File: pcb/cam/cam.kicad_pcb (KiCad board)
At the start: 4 copper layers, 75 x 65 mm, 116 parts, among them J1 Conn_Coaxial, J2 Power In, J3 PRGR, J4 Conn_01x24_Male, J5 SIM_Card, J6 Conn_Coaxial, J7 JTAG, Q1 IRLML6402, U1 TPS22810, U10 W25Q128JVS, U11 LY68L6400, U12 SRV05-4, U13 SIM800C, U2 FDC610, U3 XC6206-12, U4 XC6206-28, U5 LTC3103, U6 INA226, U7 ESP32-S2, U8 MP2307, Y1 32.768kHz, Y2 40Mhz

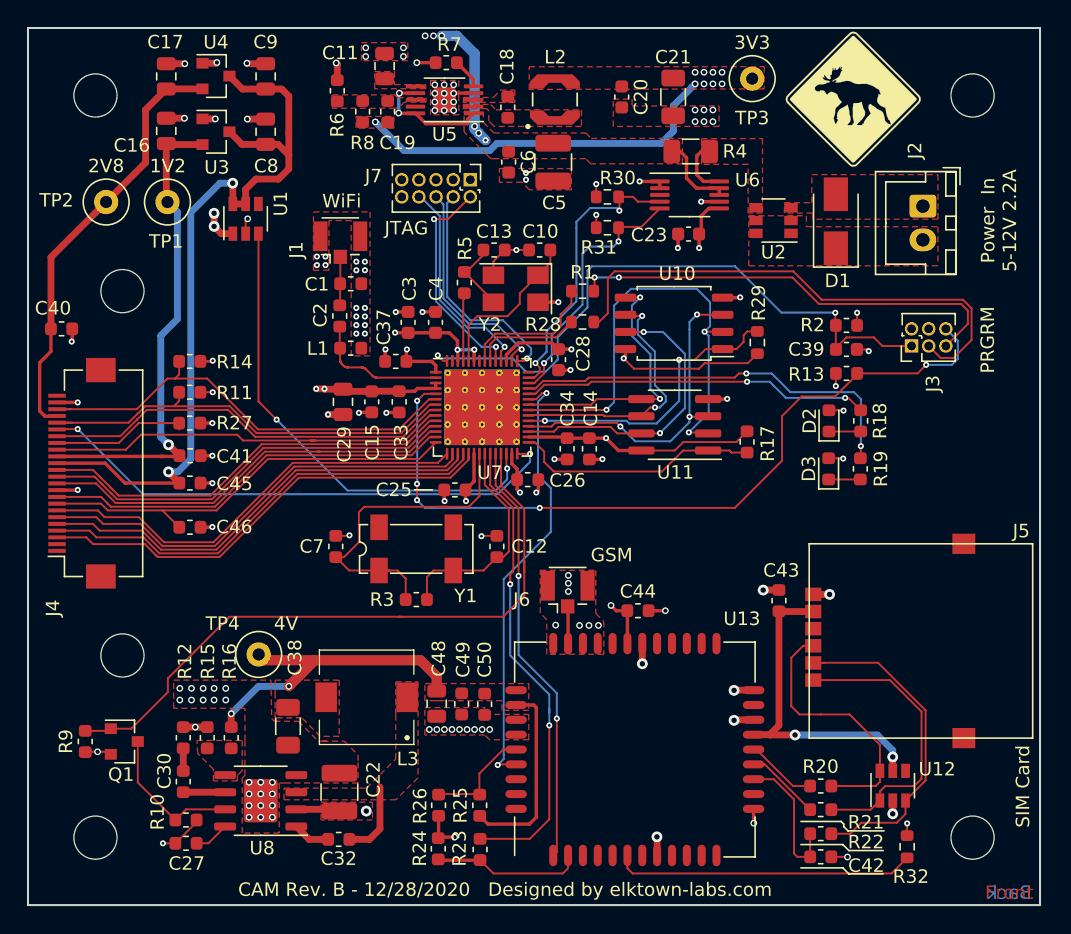
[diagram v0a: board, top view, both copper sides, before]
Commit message: Migrated to KiCad7
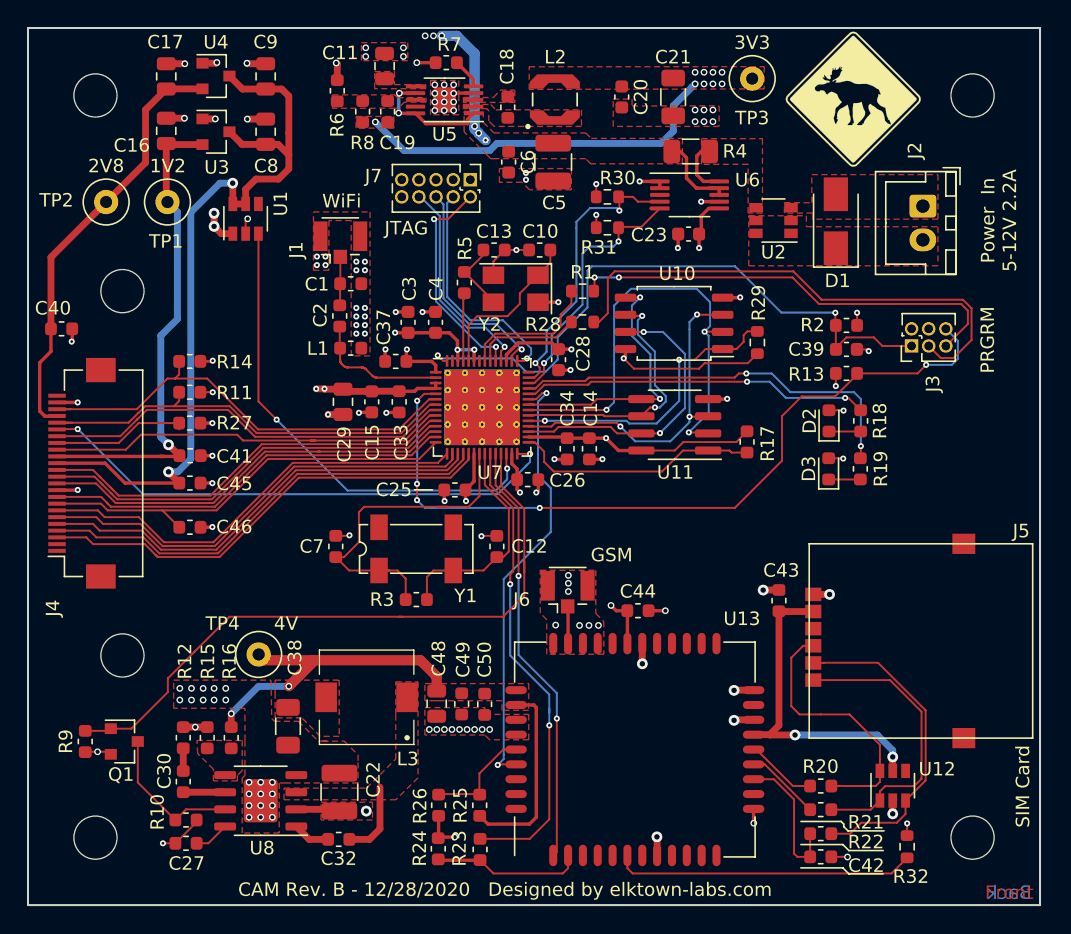
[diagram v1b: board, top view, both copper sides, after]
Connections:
- net ~RST renamed ~{RST}
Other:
- net class Default removed
- net class Power removed
